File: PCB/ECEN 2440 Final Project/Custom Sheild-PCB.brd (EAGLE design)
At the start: 63.2 x 102.9 mm, 10 parts

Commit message: prettyfy schematic. vague shield board layout.
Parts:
- removed JP1: (no value), pinhead:1X06
- added C1, C2, C3: 500n, rcl:C0805
- added OI_1, OI_2, OI_3: (no value), pinhead:1X03
- added R3, R4, R5: 100R, rcl:R0805
- added U$4: DRA_BREAKOUT, Custom Library:DRA_BREAKOUT
- moved TEENSY 19.7 mm to (26.7, 20.3), turned to 180 degrees
- moved SJ1 15.3 mm to (39.4, 33.0), turned to 180 degrees
- moved U$2 10.8 mm to (15.2, 29.2)
- moved R1 9.16 mm to (36.8, 36.8)
- moved SD_BREAKOUT 7.41 mm to (27.9, 12.7), turned to 0 degrees
- moved R2 7.18 mm to (40.6, 36.8)
- moved BATTERY 3.81 mm to (54.6, 11.4), turned to 270 degrees
- moved U$1 3.81 mm to (16.5, 24.1)
- moved U$3 2.84 mm to (0.00, 3.81)
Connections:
- net CD1 renamed SD_CD1
- new net AUDIO_FILTERED: C3.1, R5.2, U$4.MIC_IN
- new net N$3: C1.1, R3.2, R4.1
- new net N$4: C2.1, R4.2, R5.1
- new net OI_1: OI_1.2, U$3.9.1
- new net OI_2: OI_2.2, U$3.9.2
- new net OI_3: OI_3.2, U$3.9.3
- new net PD_RADIO: U$4.PD
- new net RADIO_PD: U$3.P4.1
- net +3V3: now also OI_1.3, OI_2.3, OI_3.3; no longer JP1.6
- net AUDIO_PTT: now also U$4.PTT; no longer JP1.4
- net AUDIO_PWM: now also R3.1; no longer JP1.3
- net GND: now also C1.2, C2.2, C3.2, OI_1.1, OI_2.1, OI_3.1, U$4.GND; no longer JP1.5
- net RX_RADIO: now also U$4.RX_RADIO; no longer JP1.2
- net TX_RADIO: now also U$4.TX_RADIO; no longer JP1.1
- net VCC: now also U$4.VCC
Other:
- board size 63.2 x 102.9 mm -> 58.4 x 102.9 mm

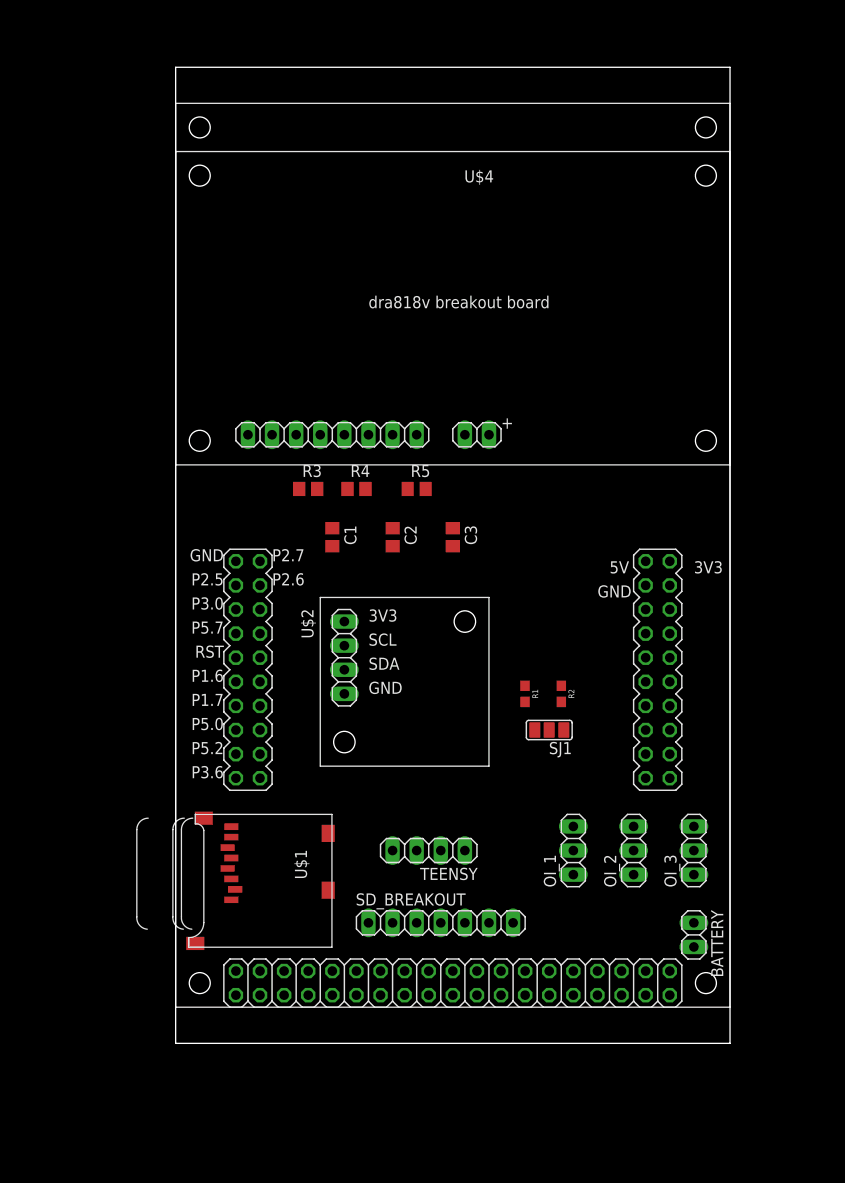
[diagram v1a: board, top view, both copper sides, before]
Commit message: Changes to board of sheild
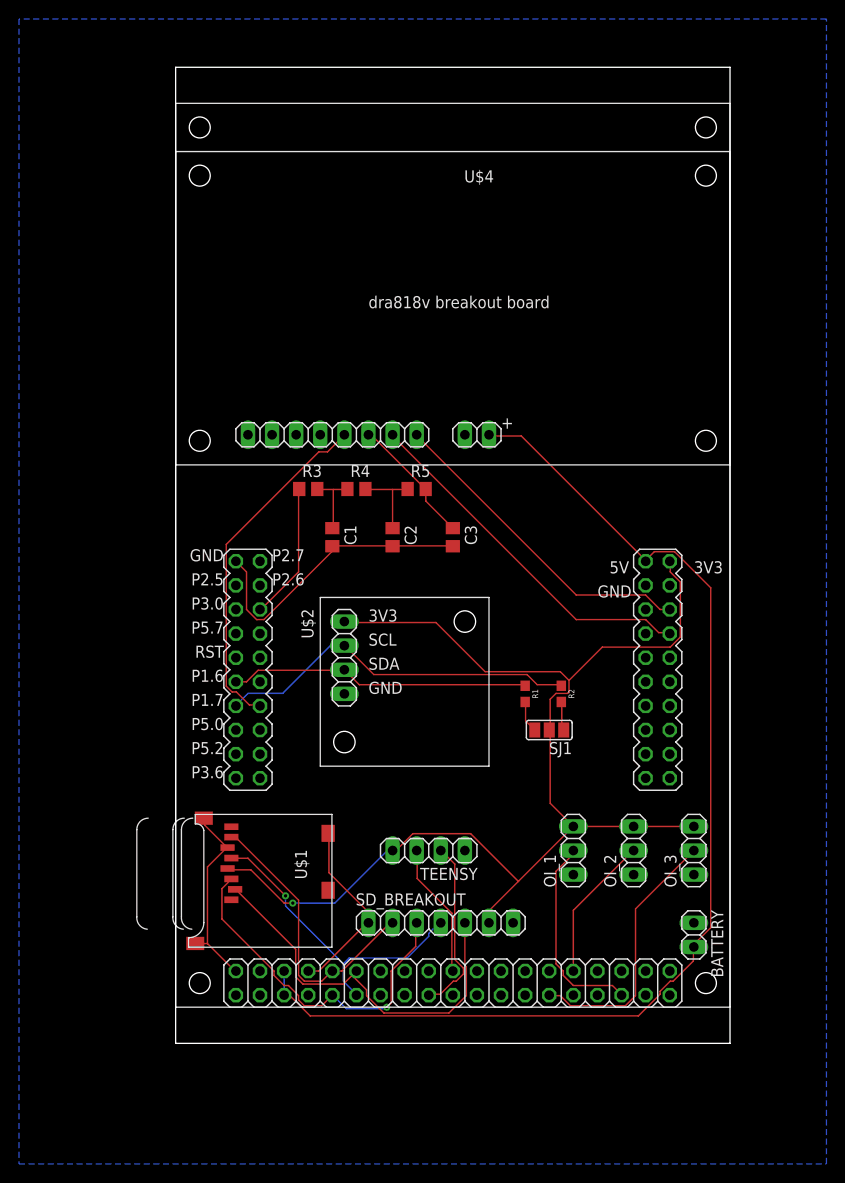
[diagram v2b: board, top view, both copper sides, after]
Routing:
- net +3V3: track 0.00 -> 130.3 mm, vias 0 -> 1
- net VCC: track 0.00 -> 120.2 mm
- net GND: track 0.00 -> 51.9 mm
- net SD_CS_SPI: track 0.00 -> 41.7 mm
- net ALT_SCL: track 0.00 -> 38.7 mm
- net RX_RADIO: track 0.00 -> 38.0 mm
- net SD_MOSI: track 0.00 -> 37.6 mm, vias 0 -> 1
- net AUDIO_PTT: track 0.00 -> 36.6 mm
- net TX_RADIO: track 0.00 -> 34.3 mm
- net SD_CLK: track 0.00 -> 33.1 mm, vias 0 -> 1
- net ALT_SDA: track 0.00 -> 31.7 mm
- net SD_MISO: track 0.00 -> 30.5 mm
- net OI_3: track 0.00 -> 27.8 mm
- net OI_1: track 0.00 -> 21.3 mm
- net SD_CD1: track 0.00 -> 19.7 mm
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- added copper zone on layer 16, net GND

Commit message: changes to the sheild board
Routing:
- net TEENSY_TX: track 14.3 -> 32.7 mm, vias 0 -> 1
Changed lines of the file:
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@@
 <contactref element="U$3" pad="9.6"/>
 <contactref element="TEENSY" pad="3"/>
-<wire x1="25.4508" y1="17.3736" x2="25.4508" y2="20.2692" width="0.1524" layer="1"/>
-<wire x1="29.1084" y1="13.716" x2="25.4508" y2="17.3736" width="0.1524" layer="1"/>
-<wire x1="29.1084" y1="7.62" x2="29.1084" y2="13.716" width="0.1524" layer="1"/>
 <wire x1="25.4508" y1="20.2692" x2="25.4" y2="20.32" width="0.1524" layer="1"/>
-<wire x1="29.1084" y1="7.62" x2="29.21" y2="7.62" width="0.1524" layer="1"/>
+<wire x1="29.21" y1="7.62" x2="27.94" y2="8.89" width="0.1524" layer="1"/>
+<wire x1="27.94" y1="8.89" x2="28.196534375" y2="10.416534375" width="0.1524" layer="1"/>
+<via x="28.196534375" y="10.416534375" extent="1-16" drill="0.35"/>
+<wire x1="28.196534375" y1="10.416534375" x2="34.292240625" y2="10.23540625" width="0.1524" layer="16"/>
+<wire x1="34.292240625" y1="10.23540625" x2="36.83" y2="10.16" width="0.1524" layer="16"/>
+<wire x1="36.83" y1="10.16" x2="39.37" y2="12.7" width="0.1524" layer="16"/>
+<wire x1="39.37" y1="12.7" x2="33.02" y2="16.51" width="0.1524" layer="16"/>
+<wire x1="33.02" y1="16.51" x2="27.94" y2="16.51" width="0.1524" layer="16"/>
+<wire x1="27.94" y1="16.51" x2="25.4" y2="20.32" width="0.1524" layer="16"/>
 </signal>
 <signal name="TEENSY_RX">

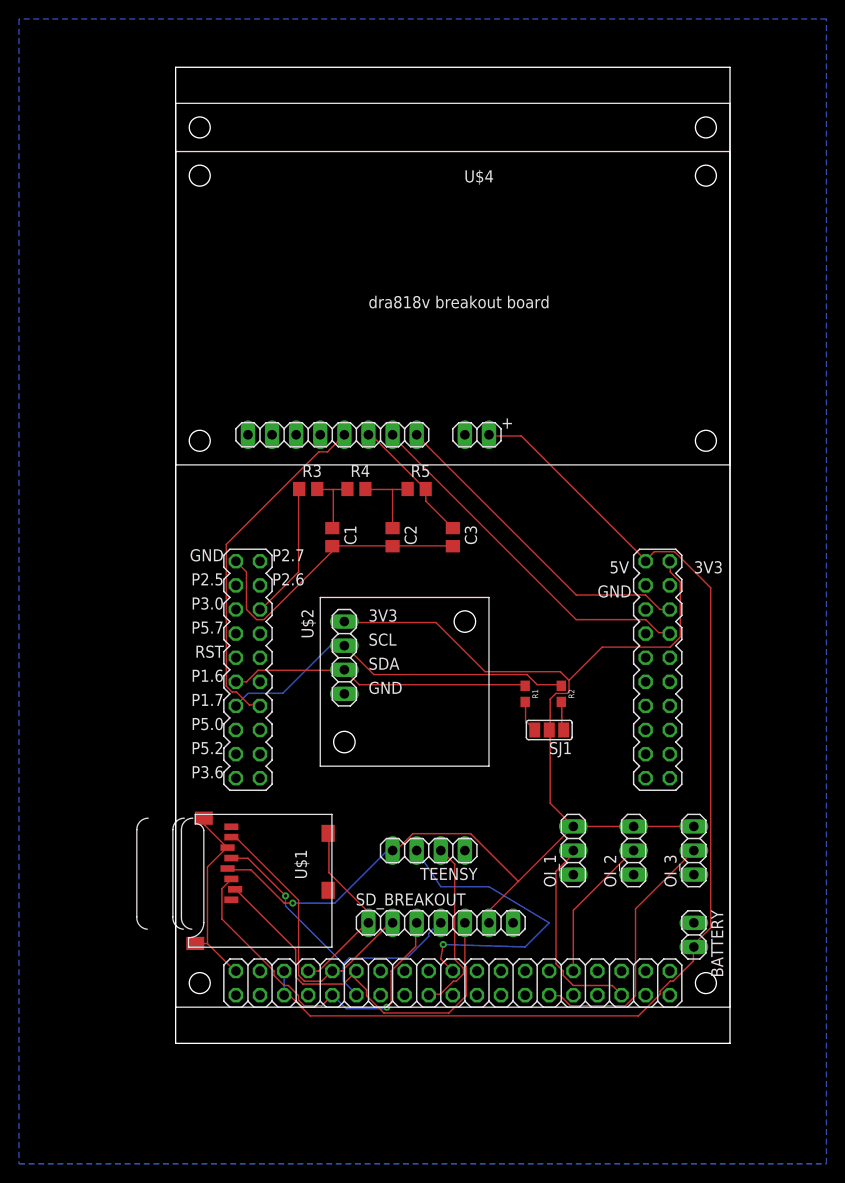
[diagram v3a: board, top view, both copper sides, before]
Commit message: changes to the traces of the shield board
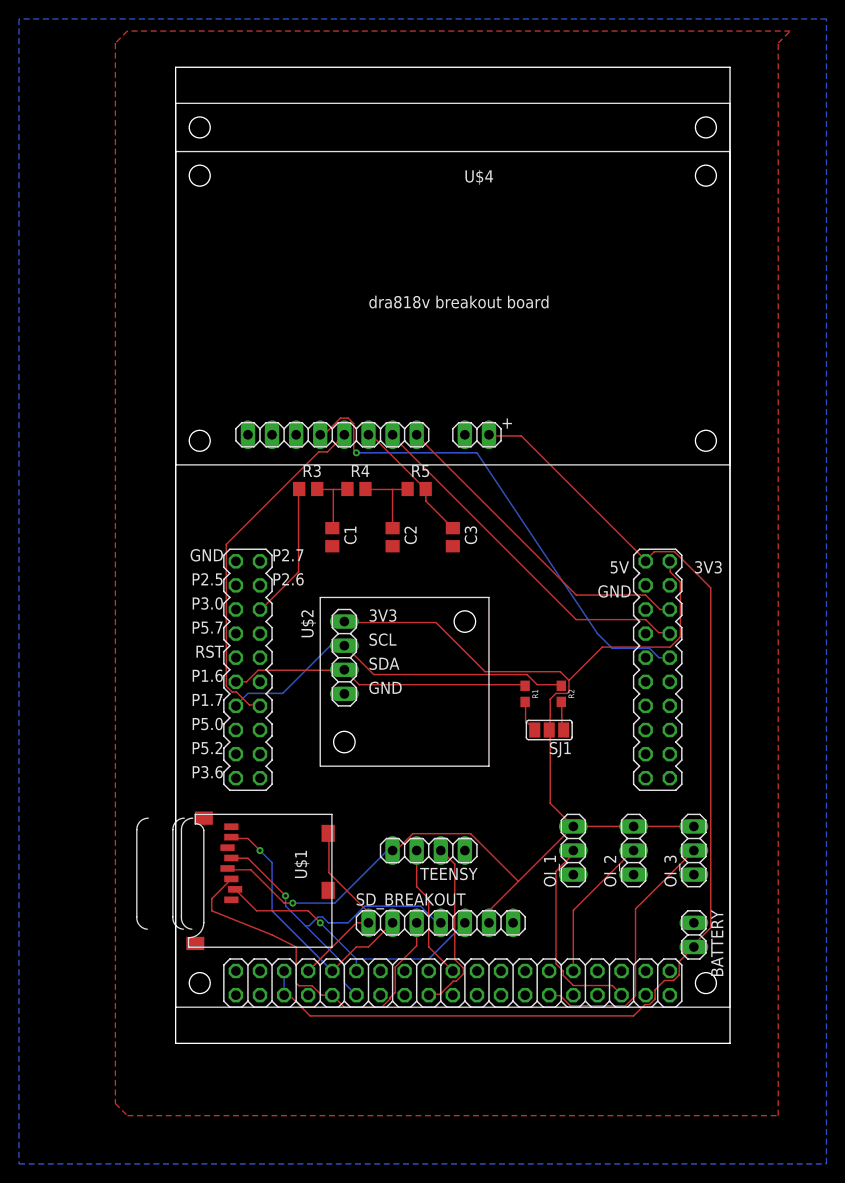
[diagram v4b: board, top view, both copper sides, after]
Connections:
- removed net RADIO_PD: U$3.P4.1
- net PD_RADIO: now also U$3.P4.1
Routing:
- net PD_RADIO: track 0.00 -> 52.0 mm, vias 0 -> 1
- net GND: track 51.9 -> 1.96 mm
- net TEENSY_TX: track 32.7 -> 14.3 mm, vias 1 -> 0
- net SD_CS_SPI: track 41.7 -> 30.2 mm, vias 0 -> 1
- net SD_CLK: track 33.1 -> 37.4 mm
- net SD_MISO: track 30.5 -> 28.8 mm, vias 0 -> 1
- net SD_MOSI: track 37.6 -> 38.4 mm, vias 1 -> 0
- added copper zone on layer 1, net GND

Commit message: changes to the traces of the sheild board
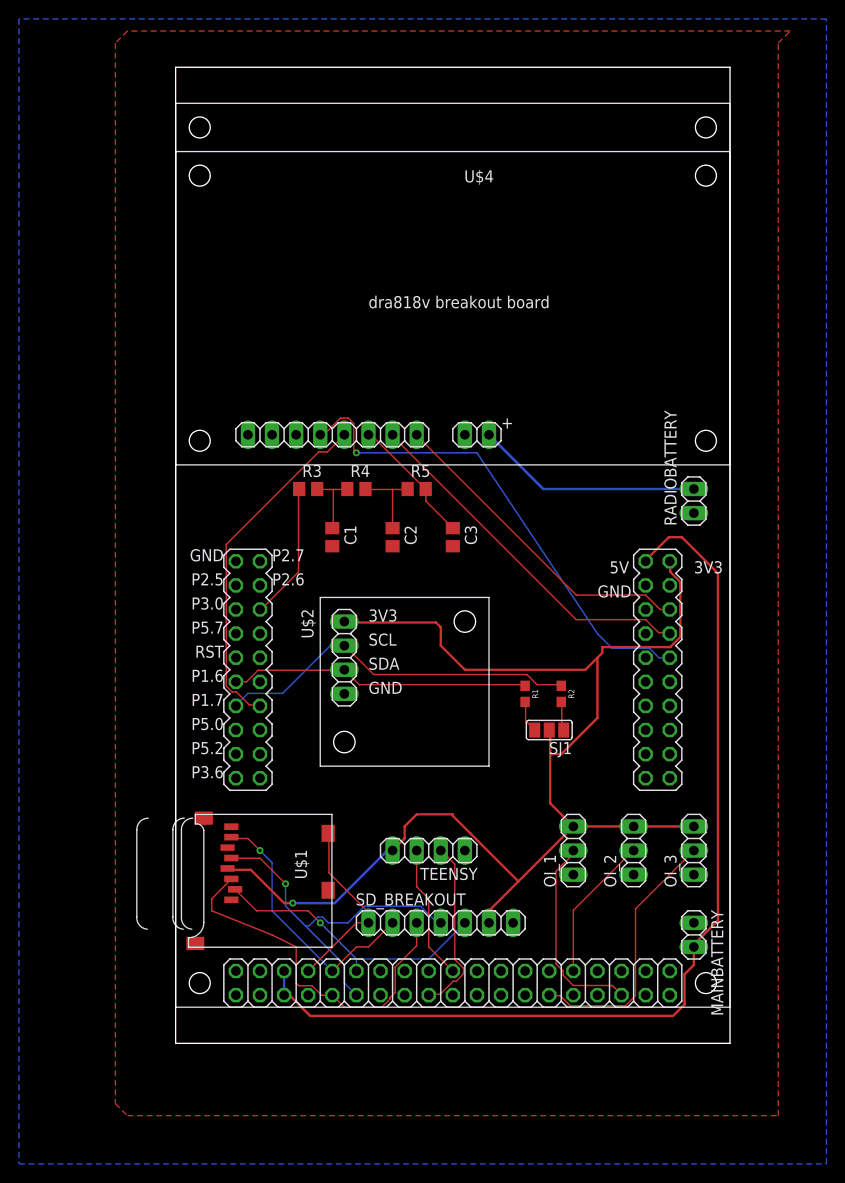
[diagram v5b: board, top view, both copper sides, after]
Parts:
- added RADIOBATTERY: (no value), pinhead:1X02
- renumbered BATTERY to MAINBATTERY
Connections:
- new net V+: RADIOBATTERY.2, U$4.VCC
- net GND: now also RADIOBATTERY.1
- net VCC: no longer U$4.VCC
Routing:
- net V+: track 0.00 -> 24.0 mm
- net VCC: track 120.7 -> 103.5 mm
- net +3V3: track 130.3 -> 139.5 mm
- net SD_CLK: track 37.4 -> 38.1 mm

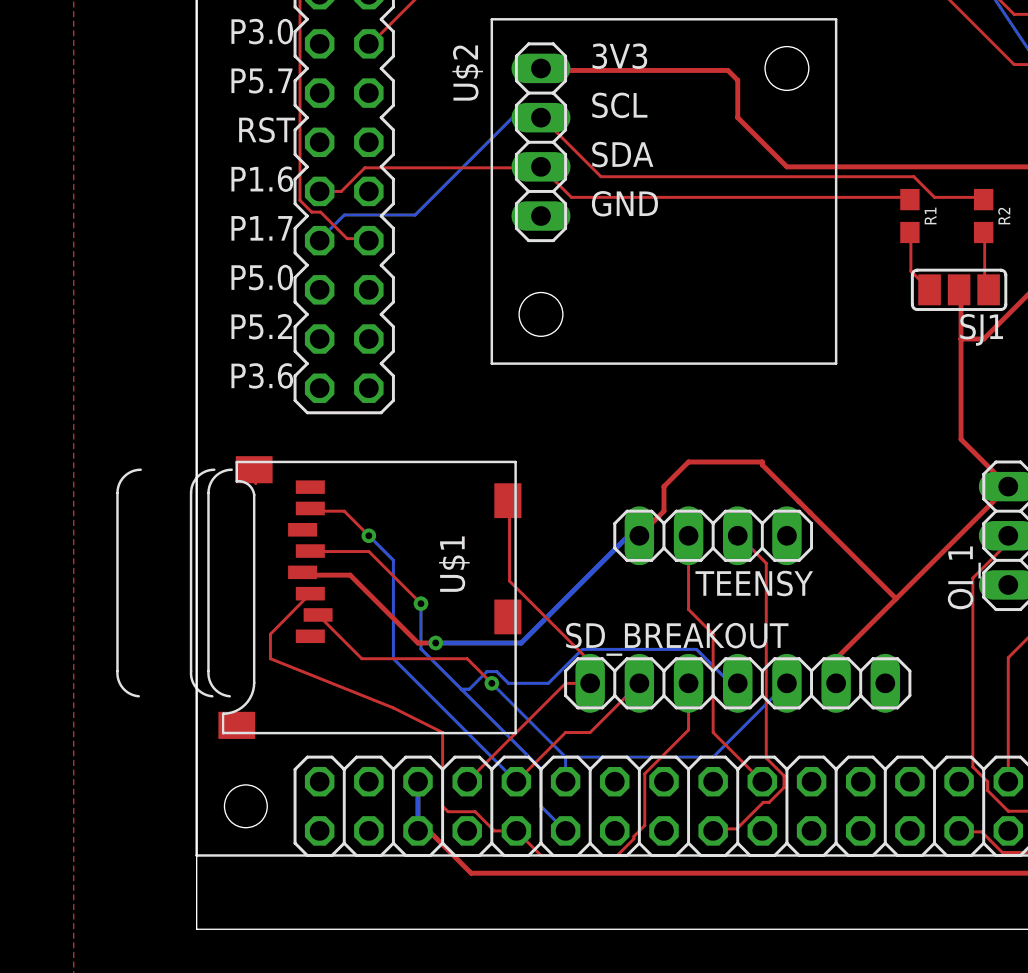
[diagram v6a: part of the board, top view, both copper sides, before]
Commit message: changes to traces on sheild board
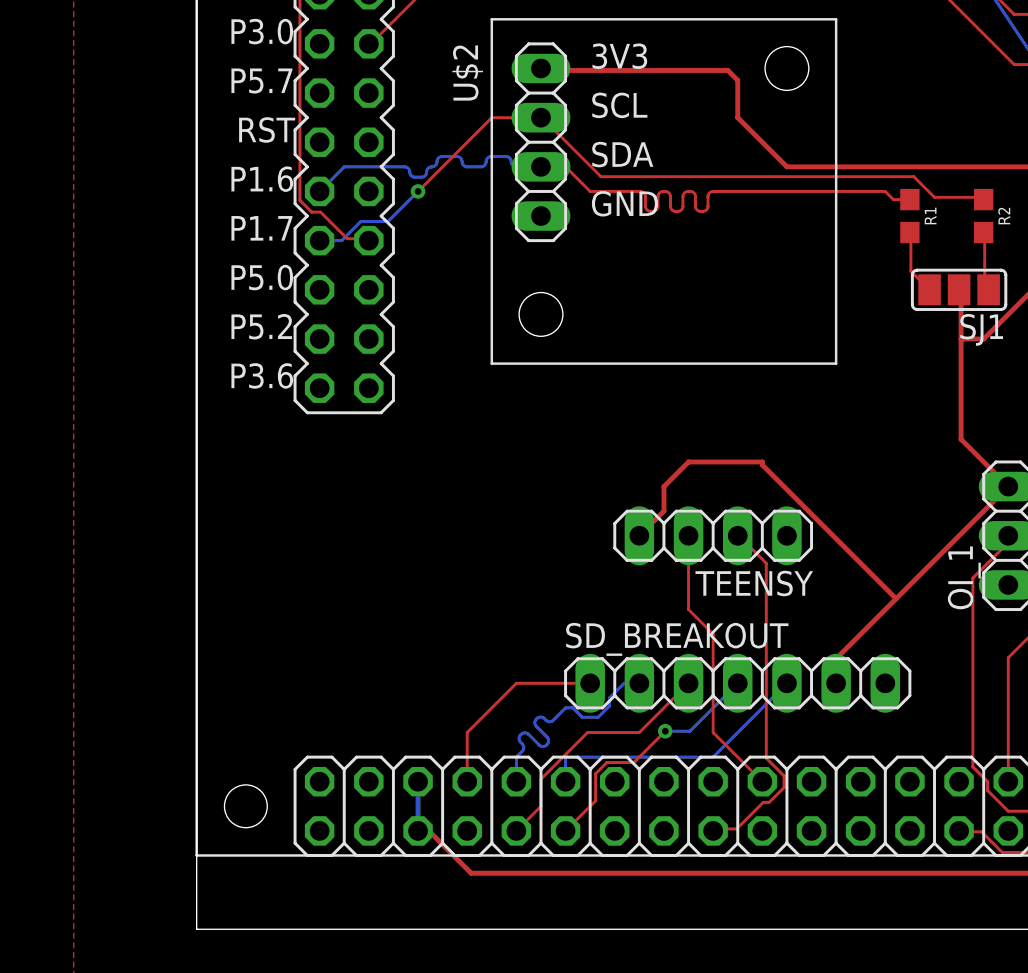
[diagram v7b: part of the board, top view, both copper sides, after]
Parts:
- removed U$1: MICROSD, adafruit:MICROSD
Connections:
- net +3V3: no longer U$1.4
- net GND: no longer U$1.6, U$1.MT1, U$1.MT2
- net SD_CD1: no longer U$1.CD1
- net SD_CLK: no longer U$1.5
- net SD_CS_SPI: no longer U$1.2
- net SD_MISO: no longer U$1.7
- net SD_MOSI: no longer U$1.3
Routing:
- net SD_MOSI: track 38.4 -> 12.9 mm
- net SD_CLK: track 38.1 -> 12.9 mm
- net +3V3: track 139.5 -> 118.9 mm, vias 1 -> 0
- net SD_MISO: track 28.8 -> 12.5 mm, vias 1 -> 0
- net SD_CS_SPI: track 30.2 -> 14.3 mm, vias 1 -> 0
- net SD_CD1: track 19.7 -> 9.94 mm
- net ALT_SDA: track 31.7 -> 37.3 mm
- net GND: track 1.96 -> 0.84 mm
- net ALT_SCL: track 38.7 -> 38.6 mm, vias 0 -> 1
